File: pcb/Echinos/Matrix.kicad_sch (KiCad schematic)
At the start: 48 parts, among them SW111 SW_Push, SW112 SW_Push, SW113 SW_Push, SW114 SW_Push, SW115 SW_Push, SW122 SW_Push, SW123 SW_Push, SW124 SW_Push, SW125 SW_Push, SW131 SW_Push, SW132 SW_Push, SW133 SW_Push, SW134 SW_Push, SW135 SW_Push, SW141 SW_Push, SW142 SW_Push, SW143 SW_Push, SW144 SW_Push, SW145 SW_Push, SW151 SW_Push, SW152 SW_Push, SW153 SW_Push, SW154 SW_Push, SW155 SW_Push

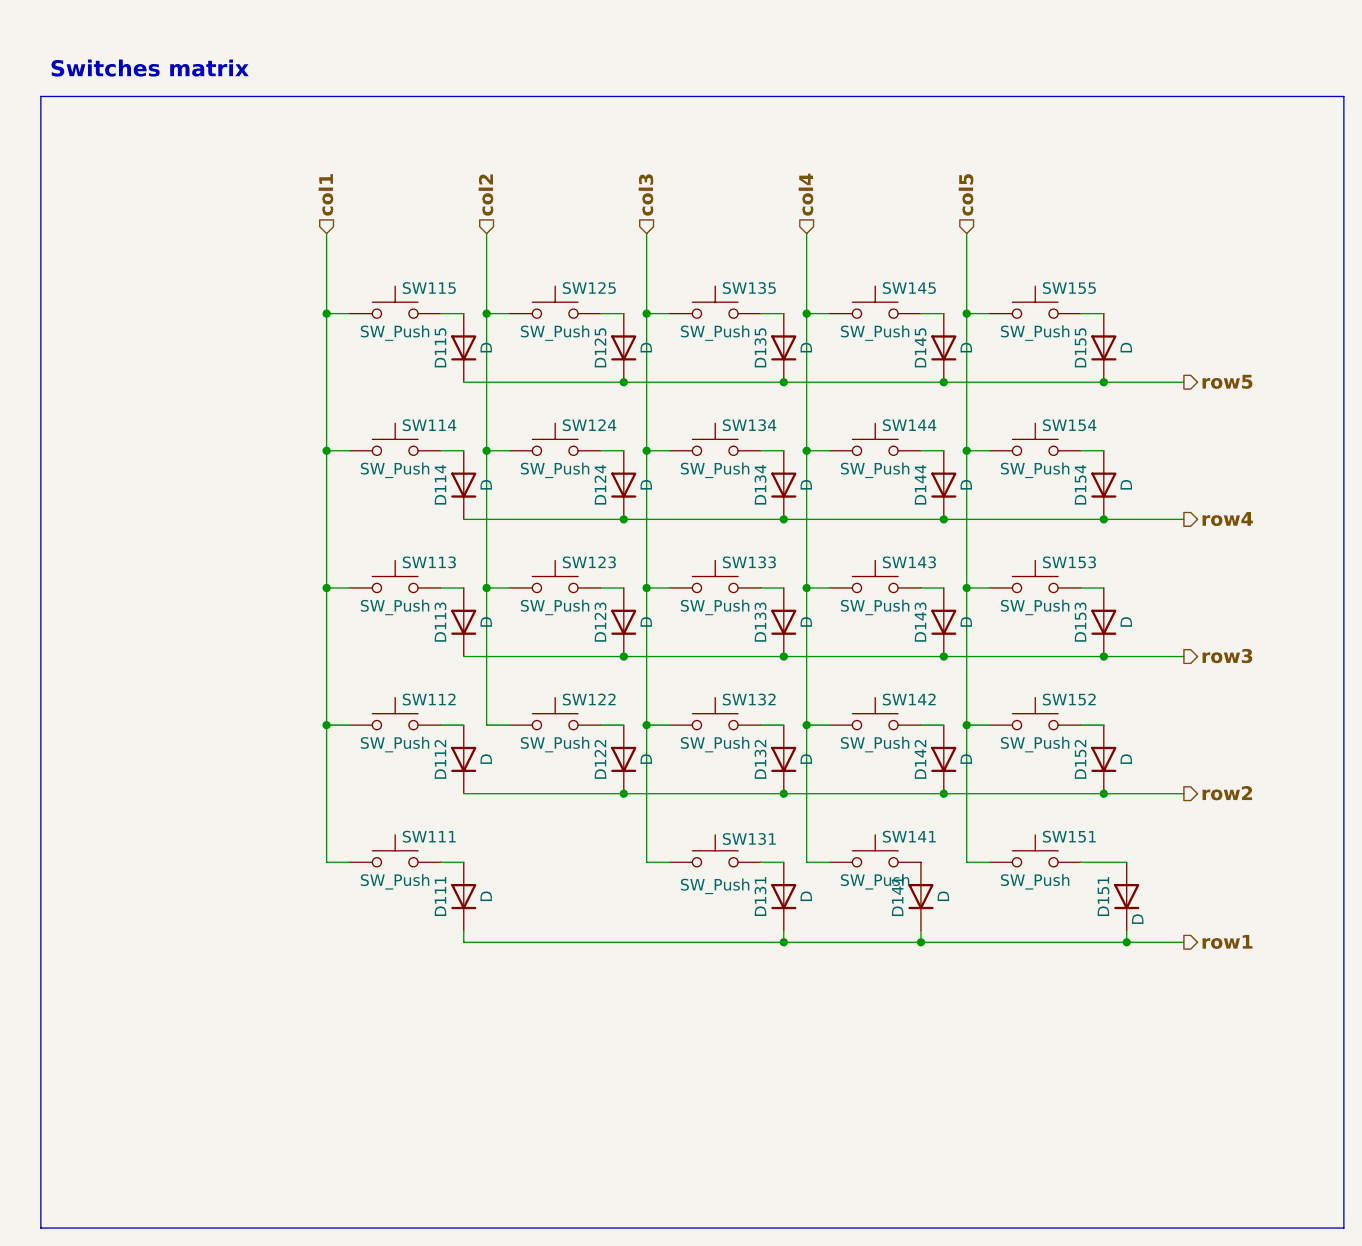
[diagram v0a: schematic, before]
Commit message: [PCB] - Save last state with on board RP2040.   - Create right side and route all components   - Component still on the bottom side to be able to merge both side for manufacturing
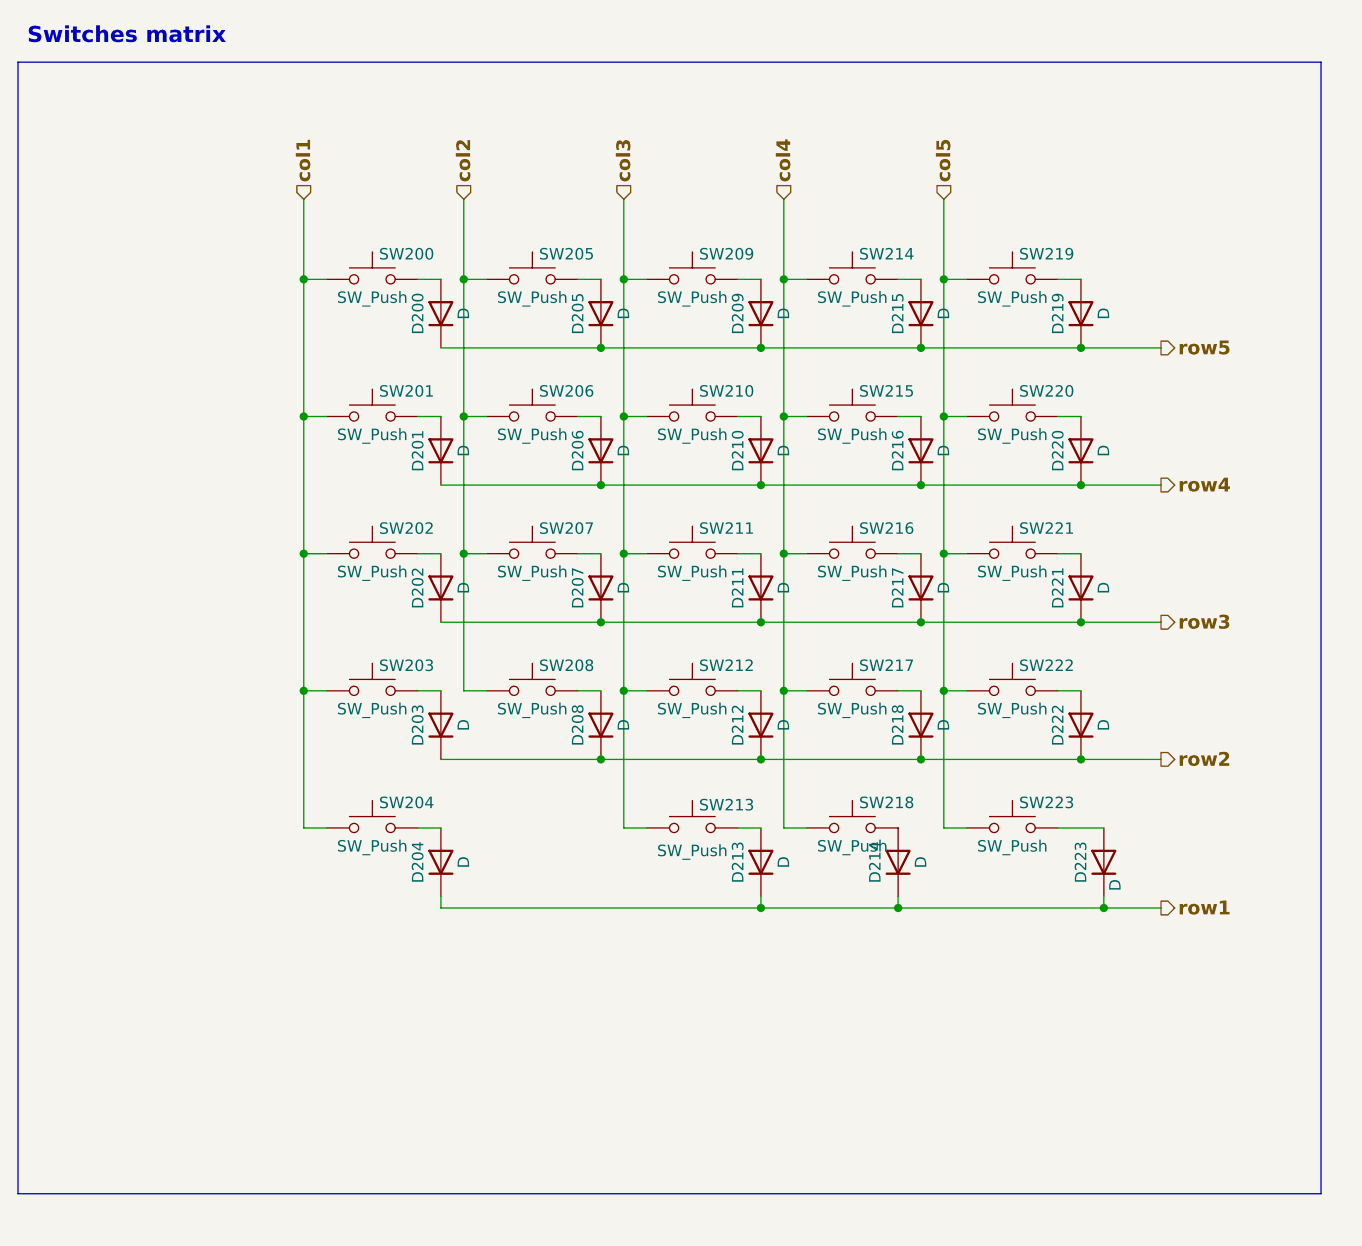
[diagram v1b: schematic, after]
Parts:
- removed D111, D112, D113, D114, D115, D122, D123, D124, D125, D131, D132, D133, D134, D135, D141, D142, D143, D144, D145, D151, D152, D153, D154, D155: D, Echinos:D_SOD123, symbol Device:D
- removed SW111, SW112, SW113, SW114, SW115, SW122, SW123, SW124, SW125, SW131, SW132, SW133, SW134, SW135, SW141, SW142, SW143, SW144, SW145, SW151, SW152, SW153, SW154, SW155: SW_Push, Echinos:SW_Choc_MX_KS33_1u_TH_hotswap, symbol Switch:SW_Push
- added D200, D201, D202, D203, D204, D205, D206, D207, D208, D209, D210, D211, D212, D213, D214, D215, D216, D217, D218, D219, D220, D221, D222, D223: D, Echinos:D_SOD123, symbol Device:D
- added SW200, SW201, SW202, SW203, SW204, SW205, SW206, SW207, SW208, SW209, SW210, SW211, SW212, SW213, SW214, SW215, SW216, SW217, SW218, SW219, SW220, SW221, SW222, SW223: SW_Push, Echinos:SW_Choc_MX_KS33_1u_TH_hotswap, symbol Switch:SW_Push
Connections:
- net col1: now also SW200.1, SW201.1, SW202.1, SW203.1, SW204.1
- net col2: now also SW205.1, SW206.1, SW207.1, SW208.1
- net col3: now also SW209.1, SW210.1, SW211.1, SW212.1, SW213.1
- net col4: now also SW214.1, SW215.1, SW216.1, SW217.1, SW218.1
- net col5: now also SW219.1, SW220.1, SW221.1, SW222.1, SW223.1
- net row1: now also D204.1 (K), D213.1 (K), D214.1 (K), D223.1 (K)
- net row2: now also D203.1 (K), D208.1 (K), D212.1 (K), D218.1 (K), D222.1 (K)
- net row3: now also D202.1 (K), D207.1 (K), D211.1 (K), D217.1 (K), D221.1 (K)
- net row4: now also D201.1 (K), D206.1 (K), D210.1 (K), D216.1 (K), D220.1 (K)
- net row5: now also D200.1 (K), D205.1 (K), D209.1 (K), D215.1 (K), D219.1 (K)
- new net: D211.2 (A), SW211.2
- new net: D214.2 (A), SW218.2
- new net: D222.2 (A), SW222.2
- new net: D215.2 (A), SW214.2
- new net: D220.2 (A), SW220.2
- new net: D218.2 (A), SW217.2
- new net: D216.2 (A), SW215.2
- new net: D200.2 (A), SW200.2
- new net: D208.2 (A), SW208.2
- new net: D206.2 (A), SW206.2
- new net: D213.2 (A), SW213.2
- new net: D207.2 (A), SW207.2
- new net: D210.2 (A), SW210.2
- new net: D217.2 (A), SW216.2
- new net: D204.2 (A), SW204.2
- new net: D205.2 (A), SW205.2
- new net: D201.2 (A), SW201.2
- new net: D209.2 (A), SW209.2
- new net: D203.2 (A), SW203.2
- new net: D212.2 (A), SW212.2
- new net: D223.2 (A), SW223.2
- new net: D219.2 (A), SW219.2
- new net: D202.2 (A), SW202.2
- new net: D221.2 (A), SW221.2
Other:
- title: Keyboard_Matrix -> Matrix (Left)

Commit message: [PCB] - Save last state with on board RP2040.   - Fix flash component orientation for JLCPCB assembly   - Add logo + version   - Add TH in flash footprint and use the same zone fill method as for RP2040 footprint   - Improve ground planes under switches (right side)   - Move unused schematics to backup folder (will be used to create keyboard modules later)   - Add manufacturer and part name (mfr)   - Mark optional parts as DNP   - Resync with official RP2040 symbol and update pins matching
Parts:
- D200, D201, D202, D203, D204, D205, D206, D207, D208, D209, D210, D211, D212, D213, D214, D215, D216, D217, D218, D219, D220, D221, D222, D223: MFR (none) -> 1N4148W; Manufacturer (none) -> Shikues
